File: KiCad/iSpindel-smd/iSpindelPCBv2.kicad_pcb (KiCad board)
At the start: 2 copper layers, 48 x 25 mm, 30 parts, among them J1 PROG, J2 PROG_con, SW1 SW_SPDT, SW2 SW_SPDT, SW3 SW_Push, U1 MIC5219-3.3, U2 GY-521, U3 TP4056-shield-6PIN, U4 DS18B20, U5 LoRa_Ra-02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

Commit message: Changed schottky size
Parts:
- D1: footprint Diodes_SMD:D_SOD-523 -> Diodes_SMD:D_SOD-323
- moved D1 0.15 mm to (146.0, 68.2)
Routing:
- net /RES: track 25.9 -> 25.3 mm
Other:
- board text added: "OFF"
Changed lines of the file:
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@@
       (net 17 /VCC_PROG))
-  )
-  (module Diodes_SMD:D_SOD-523 (layer F.Cu)
-    (at 146 68 90)
-    (descr "http://www.diodes.com/datasheets/ap02001.pdf p.144")
-    (tags "Diode SOD523")
-    (attr smd)
-    (fp_text reference D1 (at 0 -1.3 90) (layer F.SilkS) hide
-      (effects (font (size 1 1) (thickness 0.15)))
-    )
-    (fp_text value Schottky (at 0 1.4 90) (layer F.Fab) hide
-      (effects (font (size 1 1) (thickness 0.15)))
-    )
-    (fp_text user %R (at 0 -1.3 90) (layer F.Fab) hide
-      (effects (font (size 1 1) (thickness 0.15)))
-    )
-    (fp_line (start -1.15 -0.6) (end -1.15 0.6) (layer F.SilkS) (width 0.12))
-    (fp_line (start 1.25 -0.7) (end 1.25 0.7) (layer F.CrtYd) (width 0.05))
-    (fp_line (start -1.25 -0.7) (end 1.25 -0.7) (layer F.CrtYd) (width 0.05))
-    (fp_line (start -1.25 0.7) (end -1.25 -0.7) (layer F.CrtYd) (width 0.05))
-    (fp_line (start 1.25 0.7) (end -1.25 0.7) (layer F.CrtYd) (width 0.05))
-    (fp_line (start 0.1 0) (end 0.25 0) (layer F.Fab) (width 0.1))
-    (fp_line (start 0.1 -0.2) (end -0.2 0) (layer F.Fab) (width 0.1))
-    (fp_line (start 0.1 0.2) (end 0.1 -0.2) (layer F.Fab) (width 0.1))
-    (fp_line (start -0.2 0) (end 0.1 0.2) (layer F.Fab) (width 0.1))
-    (fp_line (start -0.2 0) (end -0.35 0) (layer F.Fab) (width 0.1))
-    (fp_line (start -0.2 0.2) (end -0.2 -0.2) (layer F.Fab) (width 0.1))
-    (fp_line (start 0.65 -0.45) (end 0.65 0.45) (layer F.Fab) (width 0.1))
-    (fp_line (start -0.65 -0.45) (end 0.65 -0.45) (layer F.Fab) (width 0.1))
-    (fp_line (start -0.65 0.45) (end -0.65 -0.45) (layer F.Fab) (width 0.1))
-    (fp_line (start 0.65 0.45) (end -0.65 0.45) (layer F.Fab) (width 0.1))
-    (fp_line (start 0.7 -0.6) (end -1.15 -0.6) (layer F.SilkS) (width 0.12))
-    (fp_line (start 0.7 0.6) (end -1.15 0.6) (layer F.SilkS) (width 0.12))
-    (pad 2 smd rect (at 0.7 0 270) (size 0.6 0.7) (layers F.Cu F.Paste F.Mask)
-      (net 19 "Net-(C6-Pad1)"))
-    (pad 1 smd rect (at -0.7 0 270) (size 0.6 0.7) (layers F.Cu F.Paste F.Mask)
-      (net 11 /RES))
-    (model ${KISYS3DMOD}/Diodes_SMD.3dshapes/D_SOD-523.wrl
-      (at (xyz 0 0 0))
-      (scale (xyz 1 1 1))
-      (rotate (xyz 0 0 0))
-    )
   )
   (module KiCadCustomLibs:SK12D07VG3 (layer F.Cu)
@@
     )
   )
+  (module Diodes_SMD:D_SOD-323 (layer F.Cu)
+    (at 146.025 68.15 90)
+    (descr SOD-323)
+    (tags SOD-323)
+    (attr smd)
+    (fp_text reference D1 (at 0 -1.85 90) (layer F.SilkS) hide
+      (effects (font (size 1 1) (thickness 0.15)))
+    )
+    (fp_text value Schottky (at 0.1 1.9 90) (layer F.Fab) hide
+      (effects (font (size 1 1) (thickness 0.15)))
+    )
+    (fp_text user %R (at 0 -1.85 90) (layer F.Fab) hide
+      (effects (font (size 1 1) (thickness 0.15)))
+    )
+    (fp_line (start -1.5 -0.85) (end -1.5 0.85) (layer F.SilkS) (width 0.12))
+    (fp_line (start 0.2 0) (end 0.45 0) (layer F.Fab) (width 0.1))
+    (fp_line (start 0.2 0.35) (end -0.3 0) (layer F.Fab) (width 0.1))
+    (fp_line (start 0.2 -0.35) (end 0.2 0.35) (layer F.Fab) (width 0.1))
+    (fp_line (start -0.3 0) (end 0.2 -0.35) (layer F.Fab) (width 0.1))
+    (fp_line (start -0.3 0) (end -0.5 0) (layer F.Fab) (width 0.1))
+    (fp_line (start -0.3 -0.35) (end -0.3 0.35) (layer F.Fab) (width 0.1))
+    (fp_line (start -0.9 0.7) (end -0.9 -0.7) (layer F.Fab) (width 0.1))
+    (fp_line (start 0.9 0.7) (end -0.9 0.7) (layer F.Fab) (width 0.1))
+    (fp_line (start 0.9 -0.7) (end 0.9 0.7) (layer F.Fab) (width 0.1))
+    (fp_line (start -0.9 -0.7) (end 0.9 -0.7) (layer F.Fab) (width 0.1))
+    (fp_line (start -1.6 -0.95) (end 1.6 -0.95) (layer F.CrtYd) (width 0.05))
+    (fp_line (start 1.6 -0.95) (end 1.6 0.95) (layer F.CrtYd) (width 0.05))
+    (fp_line (start -1.6 0.95) (end 1.6 0.95) (layer F.CrtYd) (width 0.05))
+    (fp_line (start -1.6 -0.95) (end -1.6 0.95) (layer F.CrtYd) (width 0.05))
+    (fp_line (start -1.5 0.85) (end 1.05 0.85) (layer F.SilkS) (width 0.12))
+    (fp_line (start -1.5 -0.85) (end 1.05 -0.85) (layer F.SilkS) (width 0.12))
+    (pad 1 smd rect (at -1.05 0 90) (size 0.6 0.45) (layers F.Cu F.Paste F.Mask)
+      (net 11 /RES))
+    (pad 2 smd rect (at 1.05 0 90) (size 0.6 0.45) (layers F.Cu F.Paste F.Mask)
+      (net 19 "Net-(C6-Pad1)"))
+    (model ${KISYS3DMOD}/Diodes_SMD.3dshapes/D_SOD-323.wrl
+      (at (xyz 0 0 0))
+      (scale (xyz 1 1 1))
+      (rotate (xyz 0 0 0))
+    )
+  )
+  (gr_text OFF (at 168.725 88.85 90) (layer B.SilkS)
+    (effects (font (size 1.2 1.2) (thickness 0.25)) (justify mirror))
+  )
   (gr_line (start 173.5 91) (end 172 91) (angle 90) (layer Edge.Cuts) (width 0.15))
   (gr_line (start 173.5 66) (end 173.5 91) (angle 90) (layer Edge.Cuts) (width 0.15))
@@
     (effects (font (size 1.6 1.7) (thickness 0.3)) (justify mirror))
   )
-  (gr_text OUT+ (at 151.1 71.47) (layer B.SilkS)
-    (effects (font (size 1 1) (thickness 0.15)) (justify mirror))
-  )
-  (gr_text GND (at 166.39 85.6) (layer B.SilkS)
+  (gr_text OUT+ (at 152.75 71.5) (layer B.SilkS)
     (effects (font (size 1 1) (thickness 0.15)) (justify mirror))
   )
@@
     (effects (font (size 1 1) (thickness 0.15)) (justify mirror))
   )
-  (gr_text TP4056 (at 157 79.04) (layer B.SilkS)
+  (gr_text TP4056 (at 159.025 78.8) (layer B.SilkS)
     (effects (font (size 1 1) (thickness 0.15)) (justify mirror))
   )
@@
   (segment (start 144.77 69.7) (end 144.05 70.42) (width 0.4) (layer F.Cu) (net 9))
   (via (at 144.77 69.7) (size 0.7) (drill 0.4) (layers F.Cu B.Cu) (net 9))
-  (segment (start 146.82 69.7) (end 144.77 69.7) (width 0.4) (layer B.Cu) (net 9))
-  (via (at 146.82 69.7) (size 0.7) (drill 0.4) (layers F.Cu B.Cu) (net 9))
-  (segment (start 149.71 69.7) (end 146.82 69.7) (width 0.4) (layer F.Cu) (net 9))
+  (segment (start 147.275 69.7) (end 144.77 69.7) (width 0.4) (layer B.Cu) (net 9))
+  (via (at 147.275 69.7) (size 0.7) (drill 0.4) (layers F.Cu B.Cu) (net 9))
+  (segment (start 149.71 69.7) (end 147.275 69.7) (width 0.4) (layer F.Cu) (net 9))
   (segment (start 150 69.41) (end 149.71 69.7) (width 0.4) (layer F.Cu) (net 9))
   (segment (start 131.25 83.2) (end 131.25 80.83) (width 0.4) (layer F.Cu) (net 10))
@@
   (segment (start 131.25 84.75) (end 131.25 83.2) (width 0.4) (layer F.Cu) (net 10))
   (segment (start 130.95 85.05) (end 131.25 84.75) (width 0.4) (layer F.Cu) (net 10))
-  (segment (start 146 68.7) (end 146 69.91) (width 0.4) (layer F.Cu) (net 11))
+  (segment (start 146.025 69.275) (end 146 69.91) (width 0.4) (layer F.Cu) (net 11))
   (segment (start 138.48 71.2) (end 137.25 69.97) (width 0.4) (layer F.Cu) (net 11))
   (segment (start 144.71 71.2) (end 138.48 71.2) (width 0.4) (layer F.Cu) (net 11))

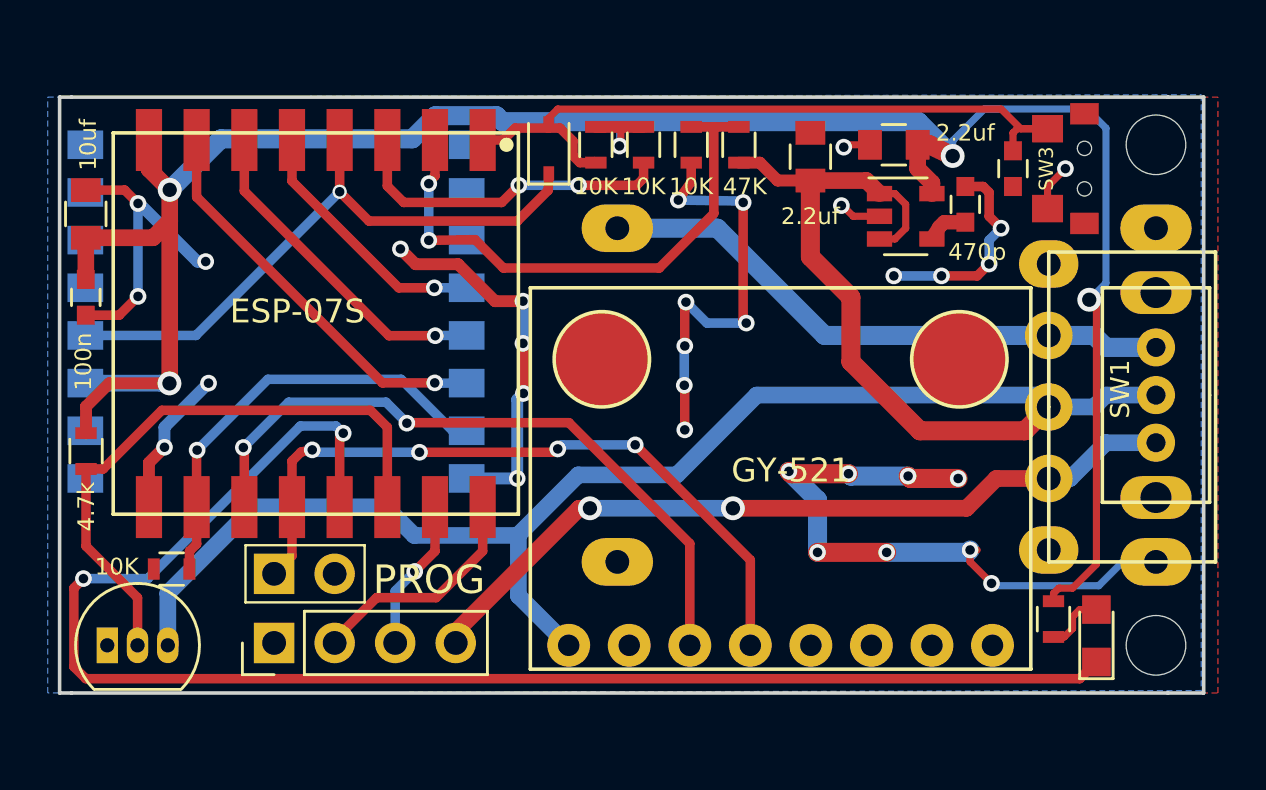
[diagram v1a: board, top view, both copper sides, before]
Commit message: Some minor adjustments to PCB. Added capacitor to DS
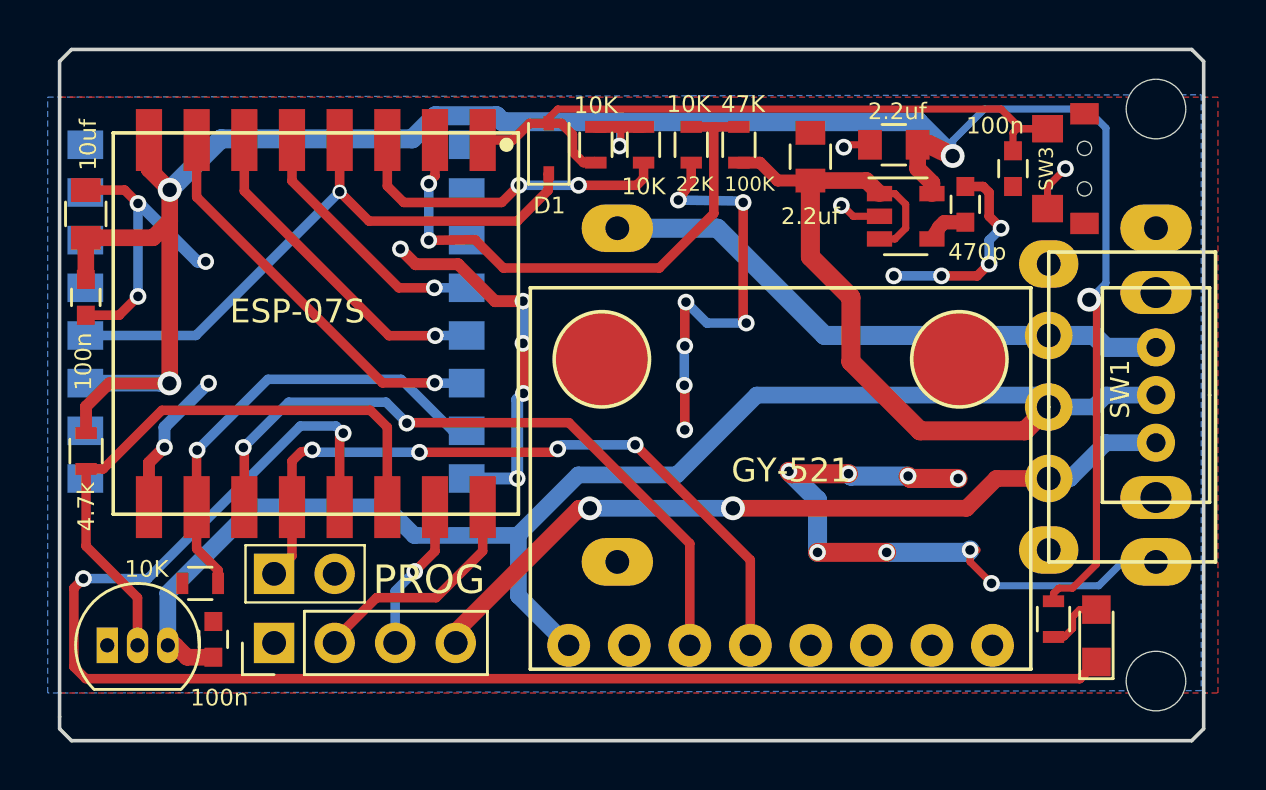
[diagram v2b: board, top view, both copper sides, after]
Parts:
- added C7: 100n, Capacitors_SMD:C_0603, F.Cu at (131.9, 88.8)
- moved REF** 1.50 mm to (171.5, 90.5)
- moved REF** 1.50 mm to (171.5, 66.5)
- moved R6 1.34 mm to (131.4, 86.4)
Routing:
- net VCC: track 82.4 -> 84.5 mm
- net /NSS: track 19.0 -> 19.8 mm
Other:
- board size 48 x 25 mm -> 48 x 29 mm
- board text added: "100K"
- board text added: "22K"
